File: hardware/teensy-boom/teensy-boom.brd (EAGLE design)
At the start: 160 x 108 mm, 147 parts, among them J1 LEFT-OUT, J2 RIGHT-OUT, J3 PHONES, J4 5-PIN-CIRCULAR-DINNEW, J5 5-PIN-CIRCULAR-DINNEW, J6 Inputs, U1 SGTL5000, U2 74hc165, U3 74hc165, U4 74hc165, U5 74hc595, U6 74hc595, U7 74hc595, U8 6N138M, U9 74AHC1G125

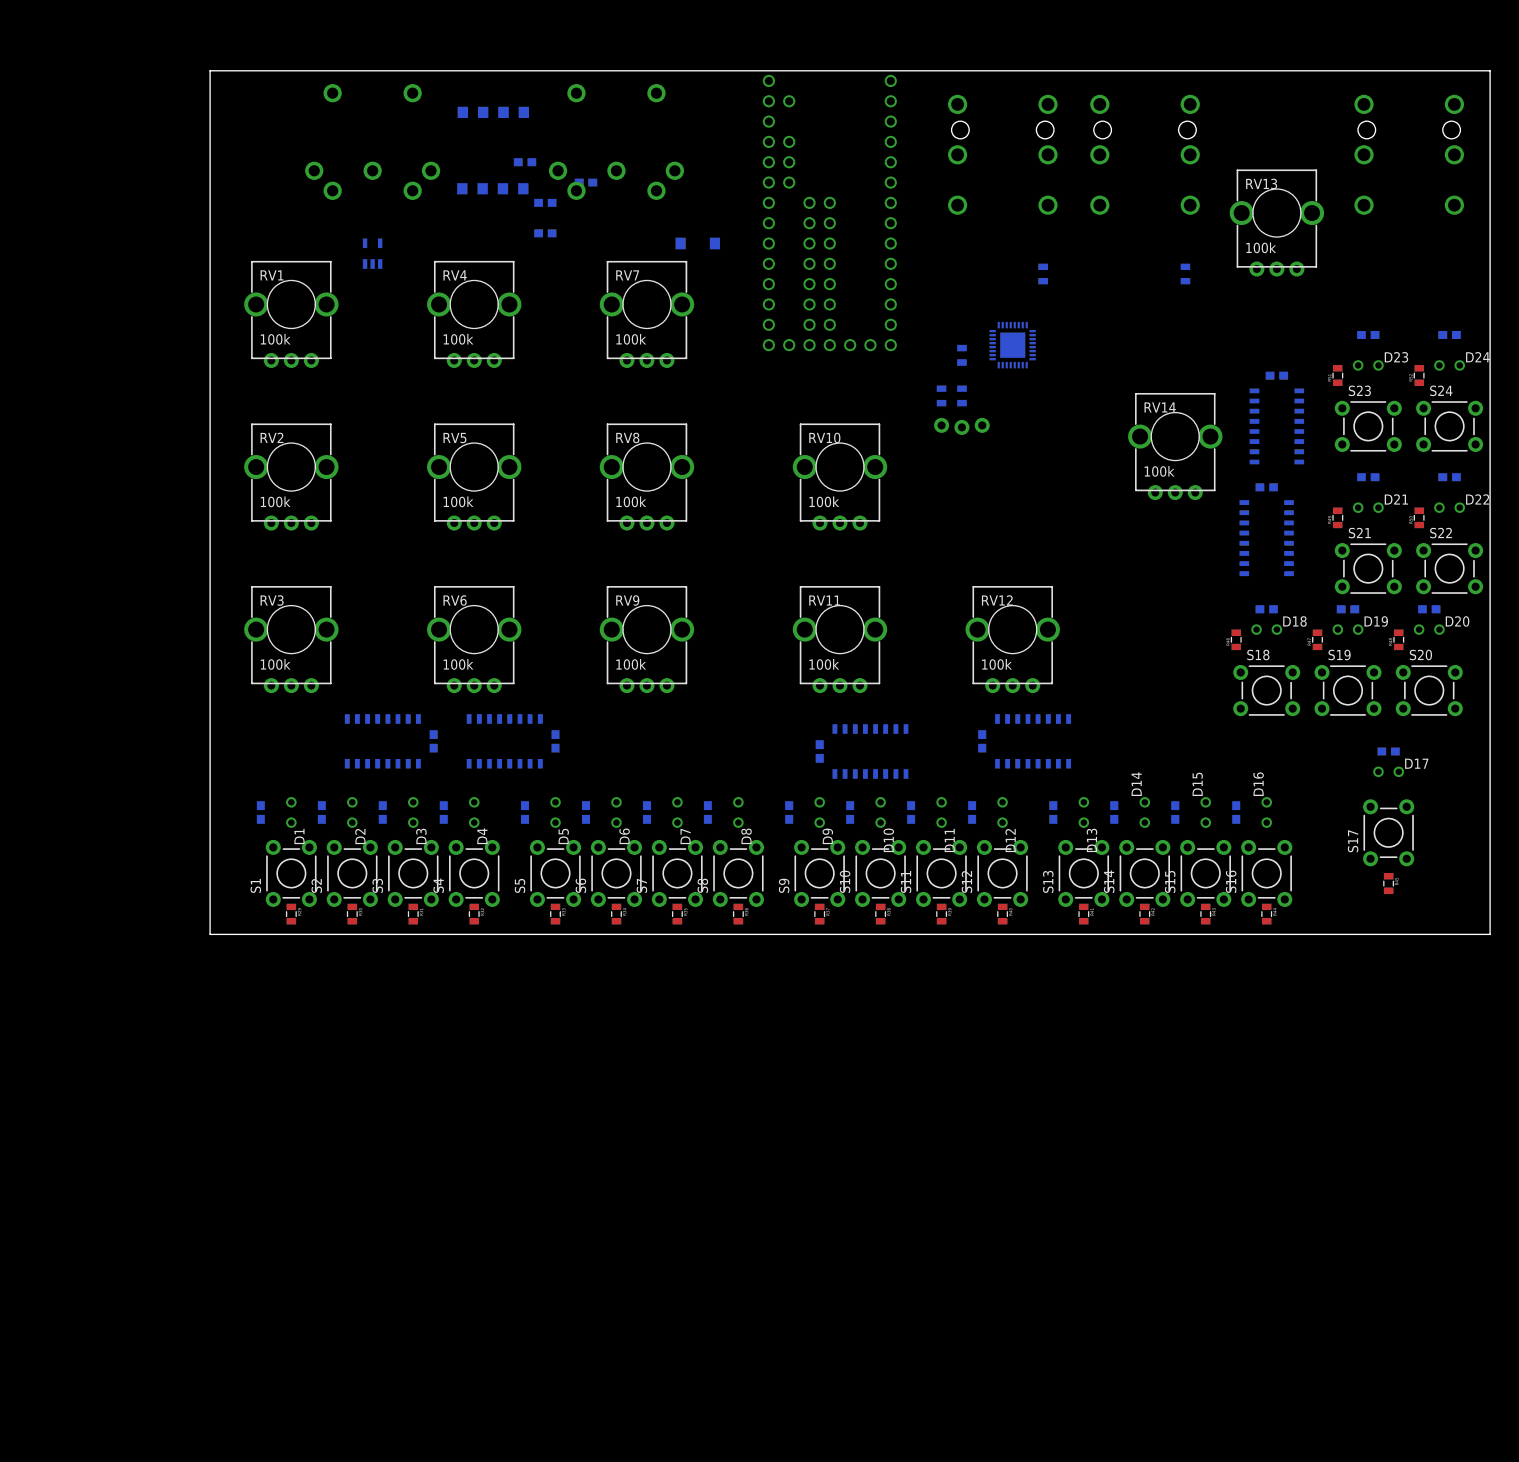
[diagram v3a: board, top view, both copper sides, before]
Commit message: Checking in WIP of large Teensy-BOOM board, so I can move to smaller one.
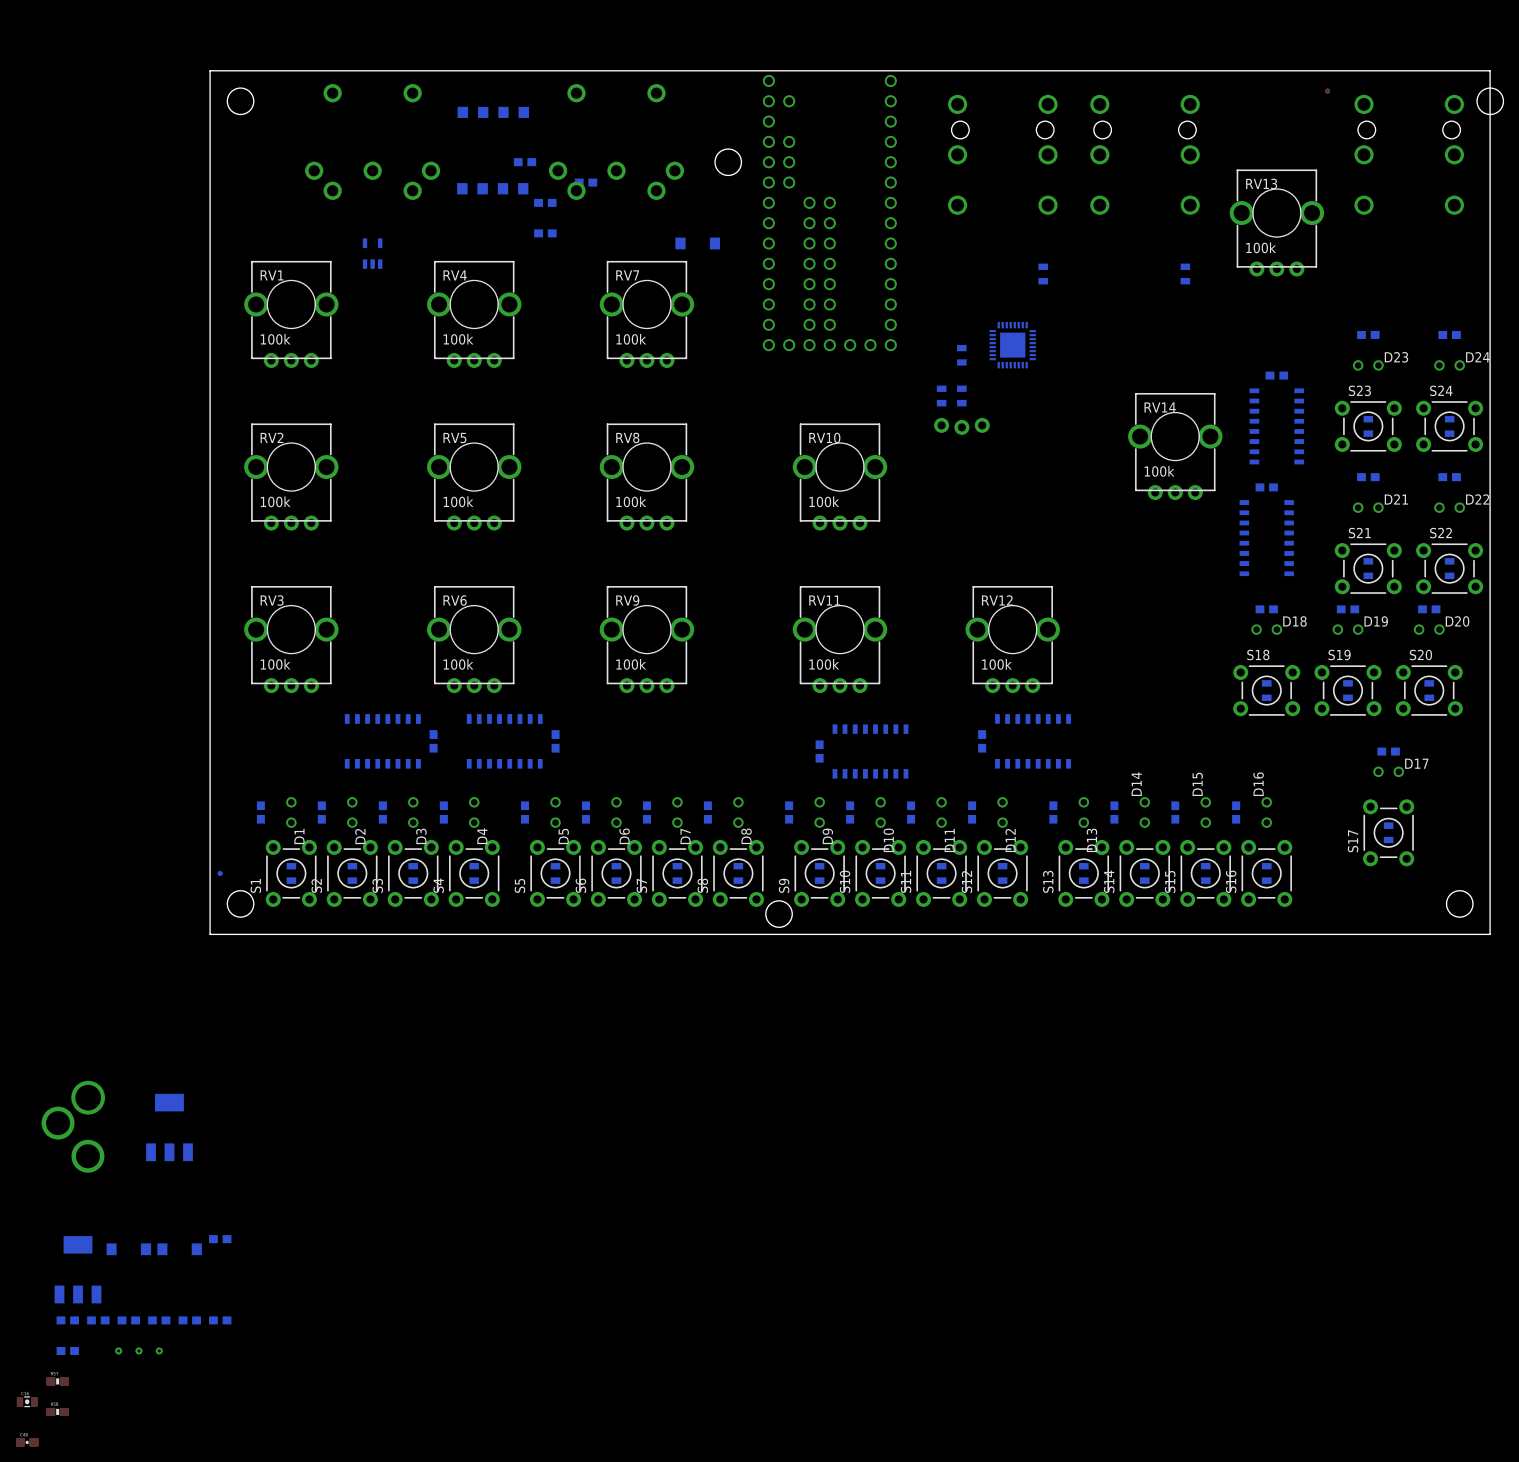
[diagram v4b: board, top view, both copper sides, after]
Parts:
- added C15, C5: 10uF, SparkFun-Capacitors:0603-CAP
- added C16: 2.2uF, SparkFun-Capacitors:0805-CAP
- added C4, C48, C6: 0.1uF, SparkFun-Capacitors:0603-CAP
- added D26, D27: MBRA140, SparkFun-DiscreteSemi:SMA-DIODE
- added FD1, FD2: FIDUCIALUFIDUCIAL, SparkFun-Aesthetics:MICRO-FIDUCIAL
- added H1, H2, H3, H4, H5, H6: STAND-OFF, SparkFun-Electromechanical:STAND-OFF
- added J10: 3.3V, SparkFun-Passives:TP_15TH
- added J11: VIN, SparkFun-Passives:TP_15TH
- added J7: POWER_JACKPTH_LOCK, SparkFun-Connectors:POWER_JACK_PTH_LOCK
- added J9: 1.8V, SparkFun-Passives:TP_15TH
- added R53: 105, SparkFun-Resistors:0603-RES
- added R54: 240, SparkFun-Resistors:0603-RES
- added R55, R56: 390, SparkFun-Resistors:0603-RES
- added R57, R58: 2.2k, SparkFun-Resistors:0603-RES
- added U10, U11: LM1117, SparkFun-PowerIC:SOT223
- moved R49 7.41 mm to (144.8, 45.7), flipped to the bottom, turned to 270 degrees
- moved R50 7.41 mm to (154.9, 45.7), flipped to the bottom, turned to 270 degrees
- moved R46 7.41 mm to (132.1, 30.5), flipped to the bottom, turned to 270 degrees
- moved R47 7.41 mm to (142.2, 30.5), flipped to the bottom, turned to 270 degrees
- moved R48 7.41 mm to (152.4, 30.5), flipped to the bottom, turned to 270 degrees
- moved R51 7.41 mm to (144.8, 63.5), flipped to the bottom, turned to 270 degrees
- moved R52 7.41 mm to (154.9, 63.5), flipped to the bottom, turned to 270 degrees
- moved R45 6.35 mm to (147.3, 12.7), flipped to the bottom
- moved R29 5.08 mm to (10.2, 7.62), flipped to the bottom
- moved R30 5.08 mm to (17.8, 7.62), flipped to the bottom
- moved R31 5.08 mm to (25.4, 7.62), flipped to the bottom
- moved R32 5.08 mm to (33.0, 7.62), flipped to the bottom
- moved R33 5.08 mm to (43.2, 7.62), flipped to the bottom
- moved R34 5.08 mm to (50.8, 7.62), flipped to the bottom
- moved R35 5.08 mm to (58.4, 7.62), flipped to the bottom
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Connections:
- new net 1.8V: C5.1, J9.P$1, R53.2, U1.30, U10.2, U10.4
- new net N$100: U3.9, U4.10
- new net N$92: U5.9, U6.14
- new net N$93: C4.1, C6.1, D26.C, D27.C, U10.3, U11.3
- new net N$94: R53.1, R55.2, U10.1
- new net N$95: R54.1, R56.2, U11.1
- new net N$96: SUB1.L10
- new net N$97: C16.1, C48.1, U1.5
- new net N$98: U6.9, U7.14
- new net N$99: U2.9, U3.10
- new net SPI-CLK: SUB1.R14, U2.2, U5.11
- new net SPI-MISO: SUB1.L12, U4.9
- new net SPI-MOSI: SUB1.L7, U5.14
- new net VIN: D27.A, J11.P$1, J7.PWR
- new net VUSB: D26.A, SUB1.BVUSB
- net 3.3V: now also C15.1, J10.P$1, R54.2, R57.2, R58.2, U1.20, U11.2, U11.4, U5.10, U6.10, U7.10
- net GND: now also C15.2, C16.2, C4.2, C48.2, C5.2, C6.2, J7.GND, J7.GNDBREAK, R55.1, R56.1, U2.15, U3.15, U4.15, U5.13, U6.13, U7.13
- net SCL: now also R58.1
- net SDA: now also R57.1
